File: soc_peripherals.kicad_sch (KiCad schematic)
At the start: 9 parts, among them SW9 TS24CA, U6 W25N01GVZEIG_C907680, U7 LSM6DS3

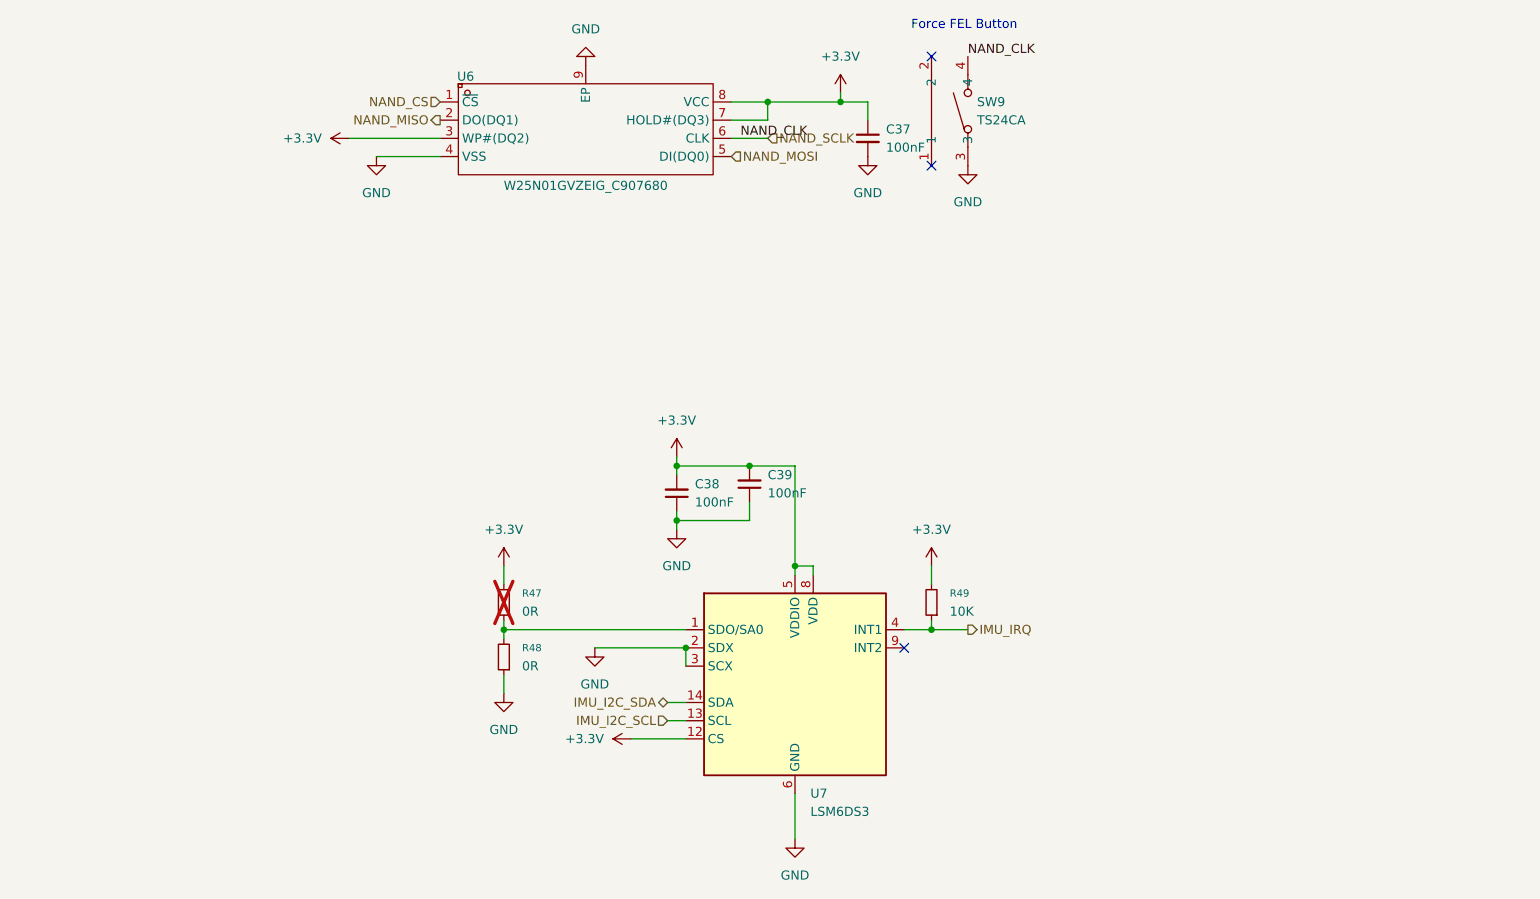
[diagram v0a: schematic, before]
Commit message: V0.3.1 bugfix
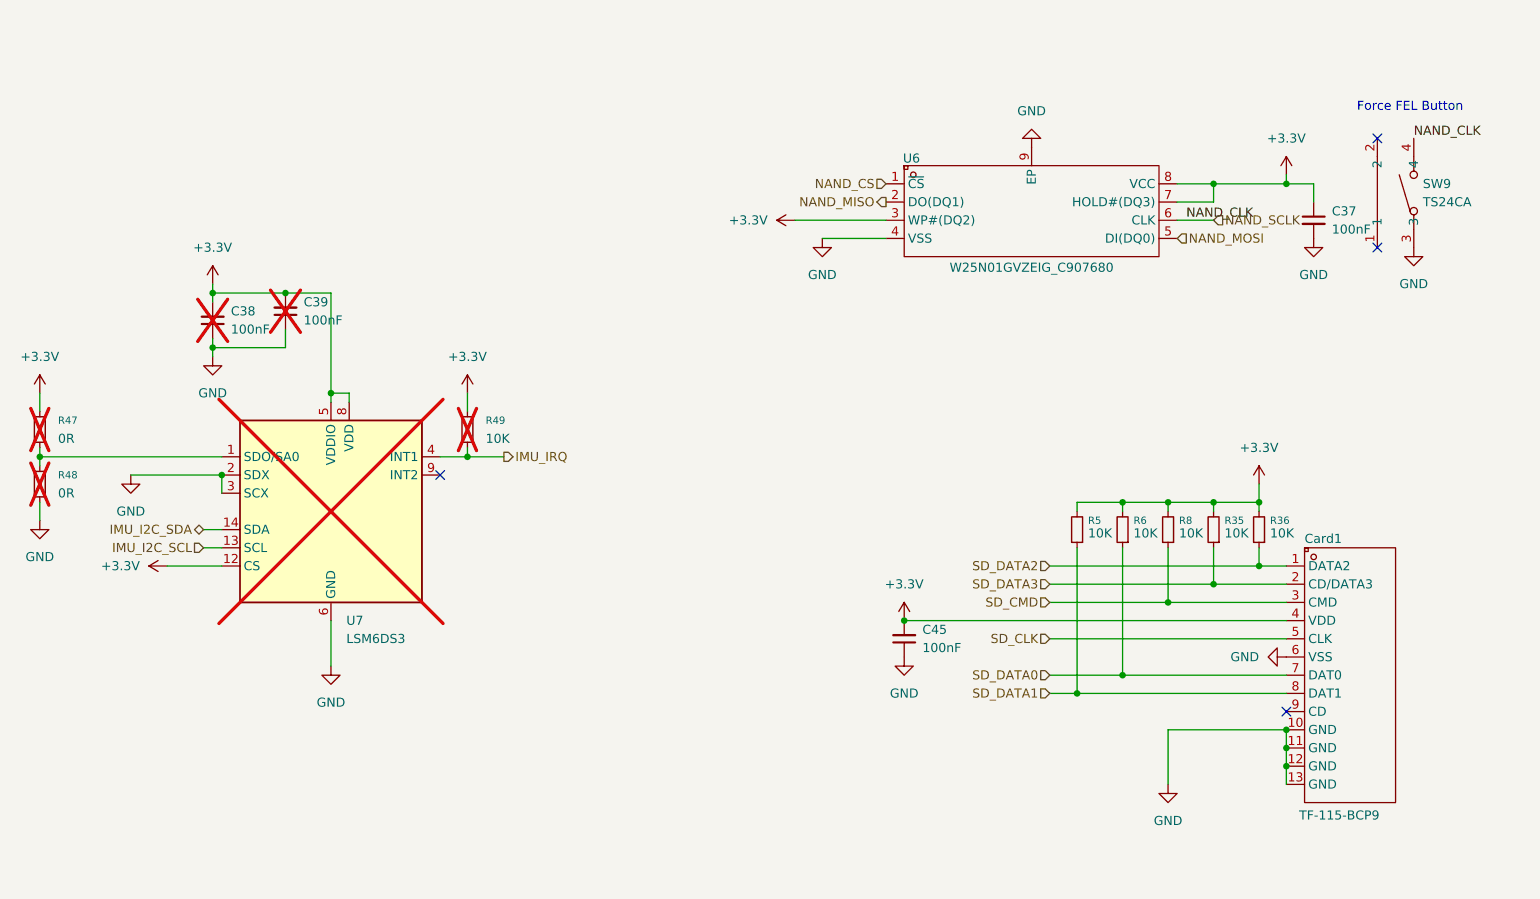
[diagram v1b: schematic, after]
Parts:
- added C45: 100nF, Capacitor_SMD:C_0603_1608Metric, symbol Device:C_Small
- added Card1: TF-115-BCP9, EasyEDA:TF-SMD_TF-115-BCP9, symbol EasyEDA:TF-115-BCP9
- added R35, R36, R5, R6, R8: 10K, Resistor_SMD:R_0603_1608Metric, symbol Device:R_Small
- C38, C39, R48, U7: 特殊说明 (none) -> 不贴装; now not fitted
- R47: 特殊说明 (none) -> 不贴装
- R49: now not fitted
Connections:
- net +3.3V: now also C45.2, Card1.4 (VDD), R35.2, R36.2, R5.2, R6.2, R8.2
- net GND: now also C45.1, Card1.10 (GND), Card1.11 (GND), Card1.12 (GND), Card1.13 (GND), Card1.6 (VSS)
- new net SD_CLK: Card1.5 (CLK)
- new net SD_CMD: Card1.3 (CMD), R8.1
- new net SD_DATA0: Card1.7 (DAT0), R6.1
- new net SD_DATA1: Card1.8 (DAT1), R5.1
- new net SD_DATA2: Card1.1 (DATA2), R36.1
- new net SD_DATA3: Card1.2 (CD/DATA3), R35.1
- no-connect marks 3 -> 4
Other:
- moved on the sheet: C37, R47, SW9, U6

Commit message: V0.5
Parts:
- removed C38, C39: 100nF, Capacitor_SMD:C_0603_1608Metric, symbol Device:C_Small
- removed R47, R48: 0R, Resistor_SMD:R_0603_1608Metric, symbol Device:R_Small
- removed R49: 10K, Resistor_SMD:R_0603_1608Metric, symbol Device:R_Small
- removed U7: LSM6DS3, Package_LGA:LGA-14_3x2.5mm_P0.5mm_LayoutBorder3x4y, symbol Sensor_Motion:LSM6DS3
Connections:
- net GND: now also SW9.1, SW9.2
- no-connect marks 4 -> 1
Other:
- moved on the sheet: C37, C45, Card1, R35, R36, R5, R6, R8, SW9, U6
